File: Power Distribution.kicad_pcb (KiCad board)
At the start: 2 copper layers, 55 x 25 mm, 16 parts, among them J1 Conn_01x02, J2 Conn_01x02, J3 Conn_01x02, J4 Conn_01x02, Q1 Q_PMOS_DGS

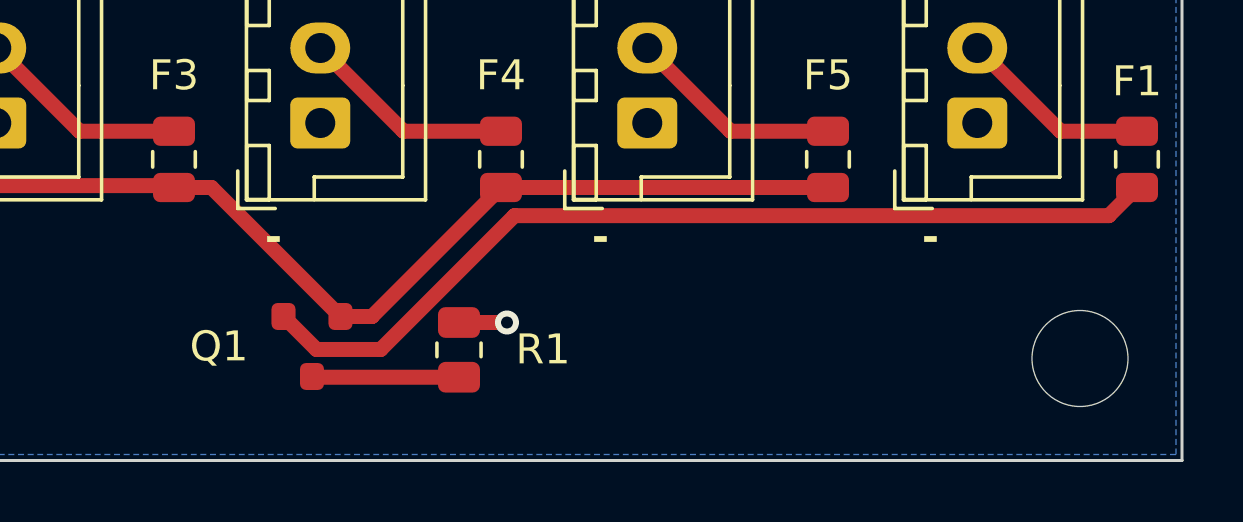
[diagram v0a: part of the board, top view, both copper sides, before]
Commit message: Add files via upload
Changed some traces to adhere to new MOSFET footprint (from web library) and meet 0.3mm distance between all components. Addeed Gerber files.
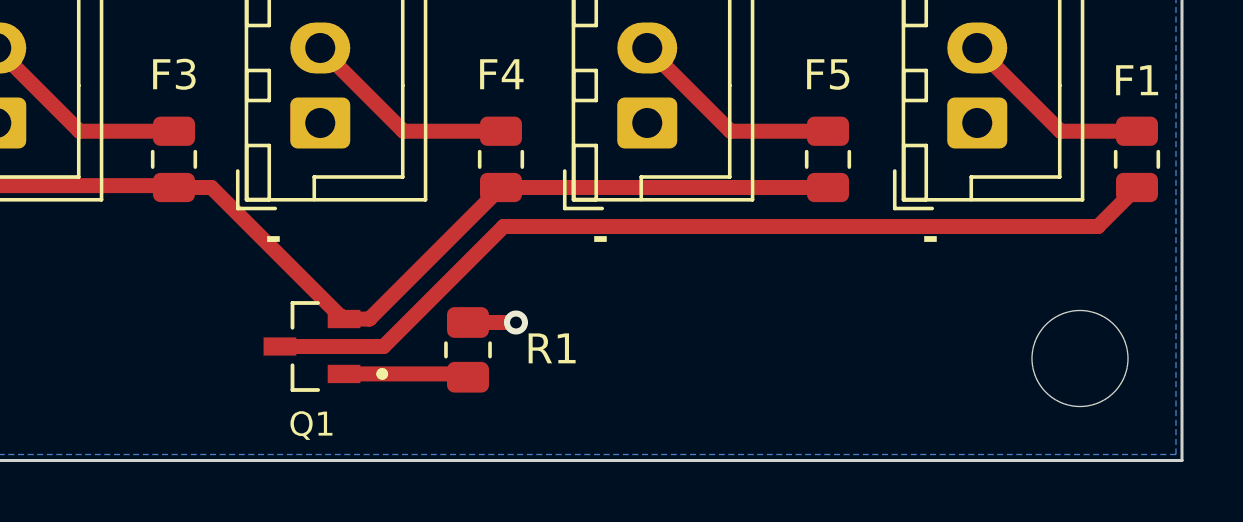
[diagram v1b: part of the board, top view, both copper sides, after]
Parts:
- Q1: footprint Transistor_Packages:SOT23_Standard -> DMP3056L-7 2:SOT91P240X110-3N
- moved R1 0.30 mm to (99.2, 93.9)
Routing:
- net Net-(Q1-G): track 4.91 -> 3.88 mm
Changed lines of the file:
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@@
 			(psa4output no)
 			(plot_black_and_white yes)
-			(plotinvisibletext no)
 			(sketchpadsonfab no)
 			(plotpadnumbers no)
@@
 			)
 		)
-		(property "Datasheet" ""
+		(property "Datasheet" "~"
 			(at 0 0 90)
 			(layer "F.Fab")
@@
 			)
 		)
-		(property "Datasheet" ""
+		(property "Datasheet" "~"
 			(at 0 0 90)
 			(layer "F.Fab")
@@
 			)
 		)
-		(property "Datasheet" ""
+		(property "Datasheet" "~"
 			(at 0 0 90)
 			(layer "F.Fab")
@@
 		)
 	)
-	(footprint "Transistor_Packages:SOT23_Standard"
+	(footprint "DMP3056L-7 2:SOT91P240X110-3N"
 		(layer "F.Cu")
 		(at 94 93.8 180)
 		(property "Reference" "Q1"
-			(at 3.1 0 0)
-			(unlocked yes)
+			(at 0 -2.6 0)
 			(layer "F.SilkS")
 			(effects
 				(font
-					(size 1 1)
+					(size 0.8 0.8)
 					(thickness 0.15)
 				)
@@
 		)
 		(property "Value" "Q_PMOS_DGS"
-			(at 0 3 180)
-			(unlocked yes)
+			(at 4.6374 2.6064 0)
 			(layer "F.Fab")
 			(effects
 				(font
-					(size 1 1)
+					(size 0.64 0.64)
 					(thickness 0.15)
 				)
@@
 		(sheetfile "Power Distribution.kicad_sch")
 		(attr smd)
-		(fp_rect
-			(start 1.75 1.6)
-			(end -1.75 -1.6)
+		(fp_line
+			(start 0.65 1.45)
+			(end 0.65 0.625)
 			(stroke
-				(width 0.05)
-				(type default)
+				(width 0.127)
+				(type solid)
+			)
+			(layer "F.SilkS")
+		)
+		(fp_line
+			(start 0.65 1.45)
+			(end -0.205 1.45)
+			(stroke
+				(width 0.127)
+				(type solid)
+			)
+			(layer "F.SilkS")
+		)
+		(fp_line
+			(start 0.65 -1.45)
+			(end 0.65 -0.625)
+			(stroke
+				(width 0.127)
+				(type solid)
+			)
+			(layer "F.SilkS")
+		)
+		(fp_line
+			(start -0.205 -1.45)
+			(end 0.65 -1.45)
+			(stroke
+				(width 0.127)
+				(type solid)
+			)
+			(layer "F.SilkS")
+		)
+		(fp_circle
+			(center -2.34 -0.915)
+			(end -2.24 -0.915)
+			(stroke
+				(width 0.2)
+				(type solid)
 			)
 			(fill no)
+			(layer "F.SilkS")
+		)
+		(fp_line
+			(start 1.865 1.7)
+			(end 1.865 -1.7)
+			(stroke
+				(width 0.05)
+				(type solid)
+			)
 			(layer "F.CrtYd")
 		)
-		(fp_text user "${REFERENCE}"
-			(at -3.048 -2.032 180)
-			(unlocked yes)
+		(fp_line
+			(start 1.865 -1.7)
+			(end -1.865 -1.7)
+			(stroke
+				(width 0.05)
+				(type solid)
+			)
+			(layer "F.CrtYd")
+		)
+		(fp_line
+			(start -1.865 1.7)
+			(end 1.865 1.7)
+			(stroke
+				(width 0.05)
+				(type solid)
+			)
+			(layer "F.CrtYd")
+		)
+		(fp_line
+			(start -1.865 -1.7)
+			(end -1.865 1.7)
+			(stroke
+				(width 0.05)
+				(type solid)
+			)
+			(layer "F.CrtYd")
+		)
+		(fp_line
+			(start 0.65 1.45)
+			(end -0.65 1.45)
+			(stroke
+				(width 0.127)
+				(type solid)
+			)
 			(layer "F.Fab")
-			(effects
-				(font
-					(size 1 1)
-					(thickness 0.15)
-				)
+		)
+		(fp_line
+			(start 0.65 -1.45)
+			(end 0.65 1.45)
+			(stroke
+				(width 0.127)
+				(type solid)
 			)
+			(layer "F.Fab")
 		)
-		(pad "1" smd roundrect
-			(at 0.95 1 180)
-			(size 0.8 0.9)
+		(fp_line
+			(start -0.65 1.45)
+			(end -0.65 -1.45)
+			(stroke
+				(width 0.127)
+				(type solid)
+			)
+			(layer "F.Fab")
+		)
+		(fp_line
+			(start -0.65 -1.45)
+			(end 0.65 -1.45)
+			(stroke
+				(width 0.127)
+				(type solid)
+			)
+			(layer "F.Fab")
+		)
+		(fp_circle
+			(center -2.34 -0.915)
+			(end -2.24 -0.915)
+			(stroke
+				(width 0.2)
+				(type solid)
+			)
+			(fill no)
+			(layer "F.Fab")
+		)
+		(pad "1" smd rect
+			(at 1.07 0 180)
+			(size 1.09 0.61)
 			(layers "F.Cu" "F.Mask" "F.Paste")
-			(roundrect_rratio 0.25)
 			(net 7 "Net-(Q1-D)")
 			(pinfunction "D")
 			(pintype "passive")
-			(thermal_bridge_angle 45)
+			(solder_mask_margin 0.102)
 		)
-		(pad "2" smd roundrect
-			(at 0 -1 180)
-			(size 0.8 0.9)
+		(pad "2" smd rect
+			(at -1.07 -0.915 180)
+			(size 1.09 0.61)
 			(layers "F.Cu" "F.Mask" "F.Paste")
-			(roundrect_rratio 0.25)
 			(net 1 "Net-(Q1-G)")
 			(pinfunction "G")
 			(pintype "input")
-			(thermal_bridge_angle 45)
+			(solder_mask_margin 0.102)
 		)
-		(pad "3" smd roundrect
-			(at -0.95 1 180)
-			(size 0.8 0.9)
+		(pad "3" smd rect
+			(at -1.07 0.915 180)
+			(size 1.09 0.61)
 			(layers "F.Cu" "F.Mask" "F.Paste")
-			(roundrect_rratio 0.25)
 			(net 9 "Net-(Q1-S)")
 			(pinfunction "S")
 			(pintype "passive")
-			(thermal_bridge_angle 45)
+			(solder_mask_margin 0.102)
 		)
 		(embedded_fonts no)
@@
 			)
 		)
-		(property "Datasheet" ""
+		(property "Datasheet" "~"
 			(at 0 0 90)
 			(layer "F.Fab")
@@
 			)
 		)
-		(property "Datasheet" ""
+		(property "Datasheet" "~"
 			(at 0 0 90)
 			(unlocked yes)
@@
 			)
 		)
-		(property "Datasheet" ""
+		(property "Datasheet" "~"
 			(at 0 0 90)
 			(layer "F.Fab")
@@
 			)
 		)
-		(property "Datasheet" ""
+		(property "Datasheet" "~"
 			(at 0 0 90)
 			(layer "F.Fab")
@@
 	(footprint "Resistor_SMD:R_0805_2012Metric"
 		(layer "F.Cu")
-		(at 98.9 93.9125 90)
+		(at 99.2 93.9125 90)
 		(descr "Resistor SMD 0805 (2012 Metric), square (rectangular) end terminal, IPC_7351 nominal, (Body size source: IPC-SM-782 page 72, https://www.pcb-3d.com/wordpress/wp-content/uploads/ipc-sm-782a_amendment_1_and_2.pdf), generated with kicad-footprint-generator")
 		(tags "resistor")
@@
 			)
 		)
-		(property "Datasheet" ""
+		(property "Datasheet" "~"
 			(at 0 0 90)
 			(layer "F.Fab")
@@
 			)
 		)
-		(property "Datasheet" ""
+		(property "Datasheet" "~"
 			(at 0 0 90)
 			(layer "F.Fab")
@@
 	)
 	(segment
-		(start 98.9 94.825)
-		(end 94.025 94.825)
+		(start 99.09 94.715)
+		(end 95.37 94.715)
 		(width 0.5)
 		(layer "F.Cu")
@@
 	)
 	(segment
-		(start 94.025 94.825)
-		(end 94 94.8)
+		(start 99.2 94.825)
+		(end 99.09 94.715)
 		(width 0.5)
 		(layer "F.Cu")
@@
 	)
 	(segment
-		(start 98.9 93)
-		(end 100.5 93)
+		(start 99.2 93)
+		(end 100.8 93)
 		(width 0.5)
 		(layer "F.Cu")
@@
 	)
 	(via
-		(at 100.5 93)
+		(at 100.8 93)
 		(size 0.8)
 		(drill 0.4)
@@
 	)
 	(segment
-		(start 94.149 93.899)
-		(end 96.290208 93.899)
-		(width 0.5)
-		(layer "F.Cu")
-		(net 7)
-	)
-	(segment
-		(start 120.5615 89.4385)
-		(end 121.5 88.5)
+		(start 100.389208 89.8)
+		(end 120.2 89.8)
 		(width 0.5)
 		(layer "F.Cu")
@@
 	)
 	(segment
-		(start 96.290208 93.899)
-		(end 100.750708 89.4385)
+		(start 96.389208 93.8)
+		(end 100.389208 89.8)
 		(width 0.5)
 		(layer "F.Cu")
@@
 	)
 	(segment
-		(start 100.750708 89.4385)
-		(end 120.5615 89.4385)
+		(start 120.2 89.8)
+		(end 121.5 88.5)
 		(width 0.5)
 		(layer "F.Cu")
@@
 	)
 	(segment
-		(start 93.05 92.8)
-		(end 94.149 93.899)
+		(start 92.93 93.8)
+		(end 96.389208 93.8)
 		(width 0.5)
 		(layer "F.Cu")
@@
 	)
 	(segment
-		(start 100.3 88.5)
-		(end 111.2 88.5)
+		(start 95.07 92.885)
+		(end 95.915 92.885)
 		(width 0.5)
 		(layer "F.Cu")
@@
 	)
 	(segment
-		(start 94.95 92.8)
-		(end 96 92.8)
+		(start 95.915 92.885)
+		(end 100.3 88.5)
 		(width 0.5)
 		(layer "F.Cu")
@@
 	)
 	(segment
-		(start 96 92.8)
-		(end 100.3 88.5)
+		(start 94.985 92.8)
+		(end 95.07 92.885)
+		(width 0.5)
+		(layer "F.Cu")
+		(net 9)
+	)
+	(segment
+		(start 100.3 88.5)
+		(end 111.2 88.5)
 		(width 0.5)
 		(layer "F.Cu")
@@
 		(width 0.5)
 		(layer "F.Cu")
+		(net 9)
+	)
+	(segment
+		(start 94.95 92.8)
+		(end 94.985 92.8)
+		(width 0.5)
+		(layer "F.Cu")
